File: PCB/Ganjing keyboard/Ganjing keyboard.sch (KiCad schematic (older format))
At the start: 166 parts, among them J1 Conn_01x04, J2 AVR-ISP-6, SW1 Rotary_Encoder_Switch, U1 ATmega32A-PU, Y1 Crystal

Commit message: Fixing PCB error
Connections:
- net Boot: no longer R1.2
- net Reset: now also R1.2
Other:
- moved on the sheet: R1, S1, S2
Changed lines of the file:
@@
 EESchema Schematic File Version 4
-LIBS:Ganjing keyboard-cache
 EELAYER 30 0
 EELAYER END
@@
 L power:GND #PWR019
 U 1 1 5F4DA3B8
-P 4750 7300
-F 0 "#PWR019" H 4750 7050 50  0001 C CNN
-F 1 "GND" H 4755 7127 50  0000 C CNN
-F 2 "" H 4750 7300 50  0001 C CNN
-F 3 "" H 4750 7300 50  0001 C CNN
-	1    4750 7300
+P 4800 7250
+F 0 "#PWR019" H 4800 7000 50  0001 C CNN
+F 1 "GND" H 4805 7077 50  0000 C CNN
+F 2 "" H 4800 7250 50  0001 C CNN
+F 3 "" H 4800 7250 50  0001 C CNN
+	1    4800 7250
 	1    0    0    -1
 $EndComp
-Text GLabel 5450 7200 2    50   Input ~ 0
+Text GLabel 5500 7150 2    50   Input ~ 0
 Reset
 $Comp
 L Ganjing-keyboard-rescue:1825910-7-dk_Tactile-Switches S2
 U 1 1 5F4DDD6B
-P 5150 7300
-F 0 "S2" H 5150 7647 60  0000 C CNN
-F 1 "Reset" H 5150 7541 60  0000 C CNN
-F 2 "digikey-footprints:Switch_Tactile_THT_6x6mm" H 5350 7500 60  0001 L CNN
-F 3 "https://www.te.com/commerce/DocumentDelivery/DDEController?Action=srchrtrv&DocNm=1825910&DocType=Customer+Drawing&DocLang=English" H 5350 7600 60  0001 L CNN
-F 4 "450-1804-ND" H 5350 7700 60  0001 L CNN "Digi-Key_PN"
-F 5 "1825910-7" H 5350 7800 60  0001 L CNN "MPN"
-F 6 "Switches" H 5350 7900 60  0001 L CNN "Category"
-F 7 "Tactile Switches" H 5350 8000 60  0001 L CNN "Family"
-F 8 "https://www.te.com/commerce/DocumentDelivery/DDEController?Action=srchrtrv&DocNm=1825910&DocType=Customer+Drawing&DocLang=English" H 5350 8100 60  0001 L CNN "DK_Datasheet_Link"
-F 9 "/product-detail/en/te-connectivity-alcoswitch-switches/1825910-7/450-1804-ND/1731414" H 5350 8200 60  0001 L CNN "DK_Detail_Page"
-F 10 "SWITCH TACTILE SPST-NO 0.05A 24V" H 5350 8300 60  0001 L CNN "Description"
-F 11 "TE Connectivity ALCOSWITCH Switches" H 5350 8400 60  0001 L CNN "Manufacturer"
-F 12 "Active" H 5350 8500 60  0001 L CNN "Status"
-	1    5150 7300
+P 5200 7250
+F 0 "S2" H 5200 7597 60  0000 C CNN
+F 1 "Reset" H 5200 7491 60  0000 C CNN
+F 2 "digikey-footprints:Switch_Tactile_THT_6x6mm" H 5400 7450 60  0001 L CNN
+F 3 "https://www.te.com/commerce/DocumentDelivery/DDEController?Action=srchrtrv&DocNm=1825910&DocType=Customer+Drawing&DocLang=English" H 5400 7550 60  0001 L CNN
+F 4 "450-1804-ND" H 5400 7650 60  0001 L CNN "Digi-Key_PN"
+F 5 "1825910-7" H 5400 7750 60  0001 L CNN "MPN"
+F 6 "Switches" H 5400 7850 60  0001 L CNN "Category"
+F 7 "Tactile Switches" H 5400 7950 60  0001 L CNN "Family"
+F 8 "https://www.te.com/commerce/DocumentDelivery/DDEController?Action=srchrtrv&DocNm=1825910&DocType=Customer+Drawing&DocLang=English" H 5400 8050 60  0001 L CNN "DK_Datasheet_Link"
+F 9 "/product-detail/en/te-connectivity-alcoswitch-switches/1825910-7/450-1804-ND/1731414" H 5400 8150 60  0001 L CNN "DK_Detail_Page"
+F 10 "SWITCH TACTILE SPST-NO 0.05A 24V" H 5400 8250 60  0001 L CNN "Description"
+F 11 "TE Connectivity ALCOSWITCH Switches" H 5400 8350 60  0001 L CNN "Manufacturer"
+F 12 "Active" H 5400 8450 60  0001 L CNN "Status"
+	1    5200 7250
 	1    0    0    -1
 $EndComp
 Wire Wire Line
-	4750 7200 4750 7300
-Wire Wire Line
-	5350 7200 5450 7200
-Wire Wire Line
-	4750 7200 4950 7200
-NoConn ~ 5350 7400
-NoConn ~ 4950 7400
+	4800 7150 4800 7250
+Wire Wire Line
+	5400 7150 5450 7150
+Wire Wire Line
+	4800 7150 5000 7150
+NoConn ~ 5400 7350
+NoConn ~ 5000 7350
 $Comp
 L Ganjing-keyboard-rescue:1825910-7-dk_Tactile-Switches S1
 U 1 1 5F4E706C
-P 5150 6600
-F 0 "S1" H 5150 6947 60  0000 C CNN
-F 1 "Boot" H 5150 6841 60  0000 C CNN
-F 2 "digikey-footprints:Switch_Tactile_THT_6x6mm" H 5350 6800 60  0001 L CNN
-F 3 "https://www.te.com/commerce/DocumentDelivery/DDEController?Action=srchrtrv&DocNm=1825910&DocType=Customer+Drawing&DocLang=English" H 5350 6900 60  0001 L CNN
-F 4 "450-1804-ND" H 5350 7000 60  0001 L CNN "Digi-Key_PN"
-F 5 "1825910-7" H 5350 7100 60  0001 L CNN "MPN"
-F 6 "Switches" H 5350 7200 60  0001 L CNN "Category"
-F 7 "Tactile Switches" H 5350 7300 60  0001 L CNN "Family"
-F 8 "https://www.te.com/commerce/DocumentDelivery/DDEController?Action=srchrtrv&DocNm=1825910&DocType=Customer+Drawing&DocLang=English" H 5350 7400 60  0001 L CNN "DK_Datasheet_Link"
-F 9 "/product-detail/en/te-connectivity-alcoswitch-switches/1825910-7/450-1804-ND/1731414" H 5350 7500 60  0001 L CNN "DK_Detail_Page"
-F 10 "SWITCH TACTILE SPST-NO 0.05A 24V" H 5350 7600 60  0001 L CNN "Description"
-F 11 "TE Connectivity ALCOSWITCH Switches" H 5350 7700 60  0001 L CNN "Manufacturer"
-F 12 "Active" H 5350 7800 60  0001 L CNN "Status"
-	1    5150 6600
+P 5200 6300
+F 0 "S1" H 5200 6647 60  0000 C CNN
+F 1 "Boot" H 5200 6541 60  0000 C CNN
+F 2 "digikey-footprints:Switch_Tactile_THT_6x6mm" H 5400 6500 60  0001 L CNN
+F 3 "https://www.te.com/commerce/DocumentDelivery/DDEController?Action=srchrtrv&DocNm=1825910&DocType=Customer+Drawing&DocLang=English" H 5400 6600 60  0001 L CNN
+F 4 "450-1804-ND" H 5400 6700 60  0001 L CNN "Digi-Key_PN"
+F 5 "1825910-7" H 5400 6800 60  0001 L CNN "MPN"
+F 6 "Switches" H 5400 6900 60  0001 L CNN "Category"
+F 7 "Tactile Switches" H 5400 7000 60  0001 L CNN "Family"
+F 8 "https://www.te.com/commerce/DocumentDelivery/DDEController?Action=srchrtrv&DocNm=1825910&DocType=Customer+Drawing&DocLang=English" H 5400 7100 60  0001 L CNN "DK_Datasheet_Link"
+F 9 "/product-detail/en/te-connectivity-alcoswitch-switches/1825910-7/450-1804-ND/1731414" H 5400 7200 60  0001 L CNN "DK_Detail_Page"
+F 10 "SWITCH TACTILE SPST-NO 0.05A 24V" H 5400 7300 60  0001 L CNN "Description"
+F 11 "TE Connectivity ALCOSWITCH Switches" H 5400 7400 60  0001 L CNN "Manufacturer"
+F 12 "Active" H 5400 7500 60  0001 L CNN "Status"
+	1    5200 6300
 	1    0    0    -1
 $EndComp
-Text GLabel 5450 6500 2    50   Input ~ 0
+Text GLabel 5500 6200 2    50   Input ~ 0
 Boot
 Wire Wire Line
-	5350 6500 5400 6500
+	5000 6200 4800 6200
 Wire Wire Line
-	4950 6500 4750 6500
+	4800 6200 4800 6300
 Wire Wire Line
-	4750 6500 4750 6600
-$Comp
-L power:+5V #PWR014
-U 1 1 5F4E9317
-P 5400 6100
-F 0 "#PWR014" H 5400 5950 50  0001 C CNN
-F 1 "+5V" H 5415 6273 50  0000 C CNN
-F 2 "" H 5400 6100 50  0001 C CNN
-F 3 "" H 5400 6100 50  0001 C CNN
-	1    5400 6100
-	1    0    0    -1
-$EndComp
-$Comp
-L Device:R_Small R1
-U 1 1 5F4E9D5C
-P 5400 6300
-F 0 "R1" H 5459 6346 50  0000 L CNN
-F 1 "10k" H 5459 6255 50  0000 L CNN
-F 2 "Resistor_THT:R_Axial_DIN0204_L3.6mm_D1.6mm_P5.08mm_Horizontal" H 5400 6300 50  0001 C CNN
-F 3 "https://www.mouser.com/datasheet/2/447/Yageo_LR_MFR_1-1714151.pdf" H 5400 6300 50  0001 C CNN
-F 4 "603-MFR-12FTF52-10K" H 5400 6300 50  0001 C CNN "Field4"
-F 5 "https://www.mouser.com/ProductDetail/Yageo/MFR-12FTF52-10K?qs=oAGoVhmvjhzLlUYKKBtdYQ%3D%3D" H 5400 6300 50  0001 C CNN "Mouser link"
-	1    5400 6300
-	1    0    0    -1
-$EndComp
-Wire Wire Line
-	5400 6100 5400 6200
-Wire Wire Line
-	5400 6400 5400 6500
-Connection ~ 5400 6500
-Wire Wire Line
-	5400 6500 5450 6500
+	5450 6750 5450 6850
 Text GLabel 4200 6500 2    50   Input ~ 0
 D+
@@
 	1    0    0    -1
 $EndComp
-NoConn ~ 5350 6700
-NoConn ~ 4950 6700
+NoConn ~ 5400 6400
+NoConn ~ 5000 6400
 Text GLabel 2650 2150 2    50   Input ~ 0
 col7
@@
 L power:GND #PWR0101
 U 1 1 5F5C998A
-P 4750 6600
-F 0 "#PWR0101" H 4750 6350 50  0001 C CNN
-F 1 "GND" H 4755 6427 50  0000 C CNN
-F 2 "" H 4750 6600 50  0001 C CNN
-F 3 "" H 4750 6600 50  0001 C CNN
-	1    4750 6600
+P 4800 6300
+F 0 "#PWR0101" H 4800 6050 50  0001 C CNN
+F 1 "GND" H 4805 6127 50  0000 C CNN
+F 2 "" H 4800 6300 50  0001 C CNN
+F 3 "" H 4800 6300 50  0001 C CNN
+	1    4800 6300
 	1    0    0    -1
 $EndComp
+$Comp
+L power:+5V #PWR014
+U 1 1 5F4E9317
+P 5450 6750
+F 0 "#PWR014" H 5450 6600 50  0001 C CNN
+F 1 "+5V" H 5465 6923 50  0000 C CNN
+F 2 "" H 5450 6750 50  0001 C CNN
+F 3 "" H 5450 6750 50  0001 C CNN
+	1    5450 6750
+	1    0    0    -1
+$EndComp
+$Comp
+L Device:R_Small R1
+U 1 1 5F4E9D5C
+P 5450 6950
+F 0 "R1" H 5509 6996 50  0000 L CNN
+F 1 "10k" H 5509 6905 50  0000 L CNN
+F 2 "Resistor_THT:R_Axial_DIN0204_L3.6mm_D1.6mm_P5.08mm_Horizontal" H 5450 6950 50  0001 C CNN
+F 3 "https://www.mouser.com/datasheet/2/447/Yageo_LR_MFR_1-1714151.pdf" H 5450 6950 50  0001 C CNN
+F 4 "603-MFR-12FTF52-10K" H 5450 6950 50  0001 C CNN "Field4"
+F 5 "https://www.mouser.com/ProductDetail/Yageo/MFR-12FTF52-10K?qs=oAGoVhmvjhzLlUYKKBtdYQ%3D%3D" H 5450 6950 50  0001 C CNN "Mouser link"
+	1    5450 6950
+	1    0    0    -1
+$EndComp
+Wire Wire Line
+	5400 6200 5500 6200
+Wire Wire Line
+	5450 7050 5450 7150
+Connection ~ 5450 7150
+Wire Wire Line
+	5450 7150 5500 7150
 $EndSCHEMATC

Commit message: Updating gerbers
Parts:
- D68: value Caps lock -> Caps
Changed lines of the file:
@@
 P 10250 5850
 F 0 "D68" H 10243 6066 50  0000 C CNN
-F 1 "Caps lock" H 10243 5975 50  0000 C CNN
+F 1 "Caps" H 10243 5975 50  0000 C CNN
 F 2 "Keyboard:LED_D3.0mm" H 10250 5850 50  0001 C CNN
 F 3 "https://media.digikey.com/pdf/Data%20Sheets/Lite-On%20PDFs/LTL-4232N.pdf" H 10250 5850 50  0001 C CNN

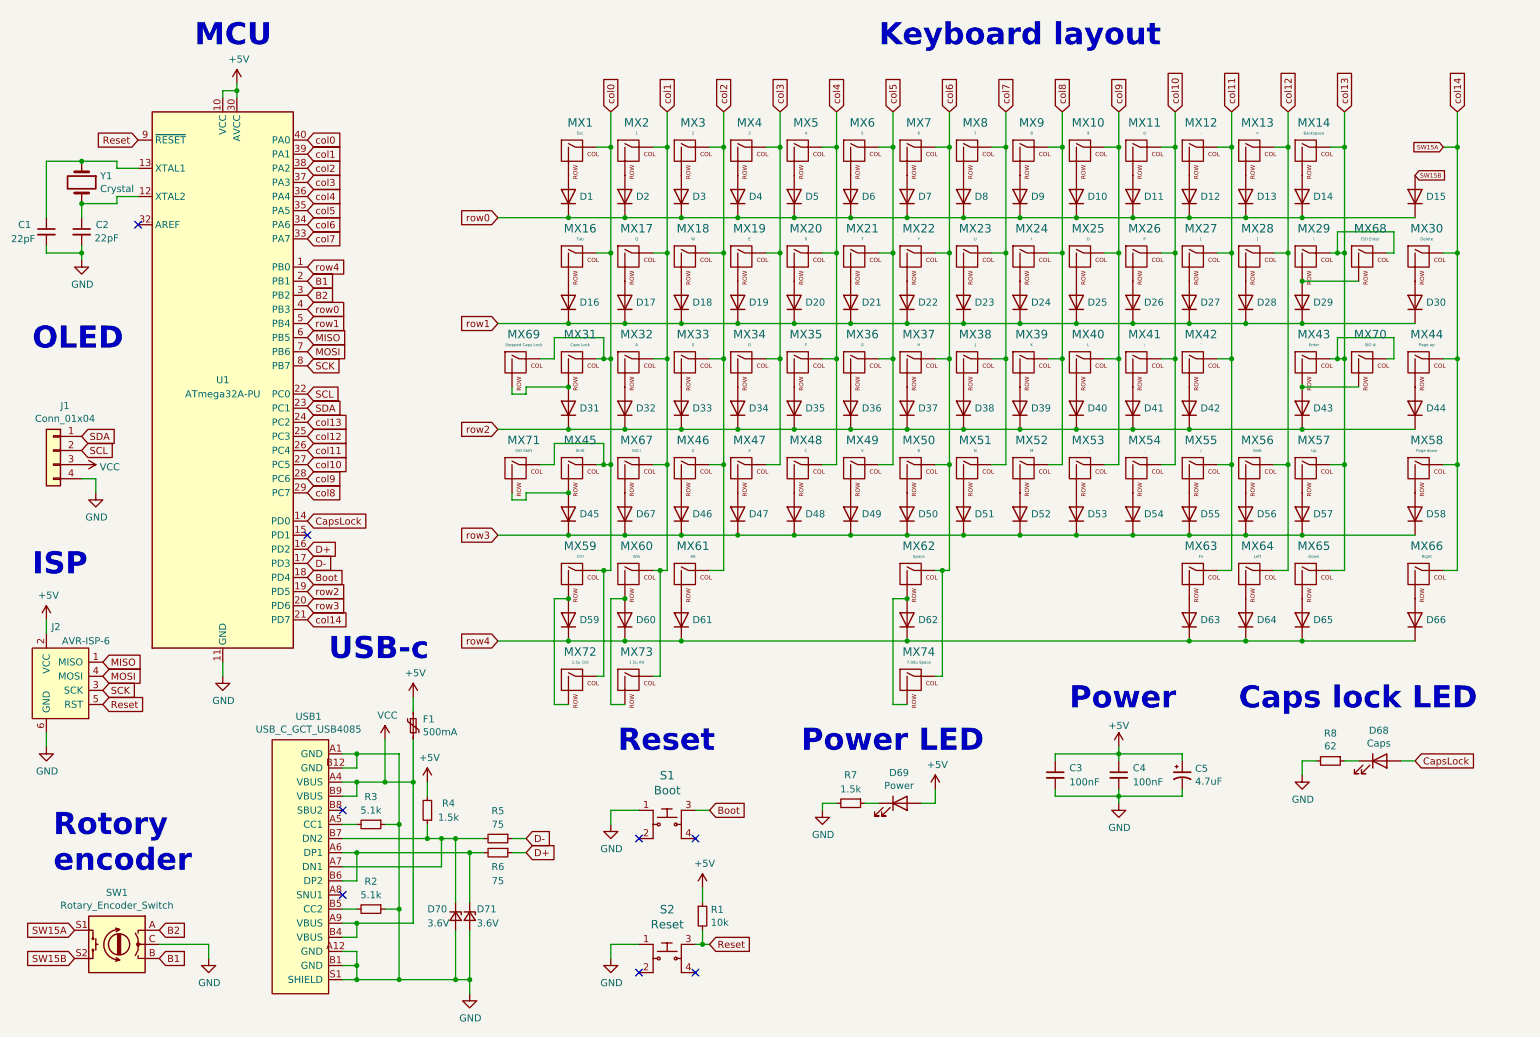
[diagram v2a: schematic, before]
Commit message: Removing caps lock LED
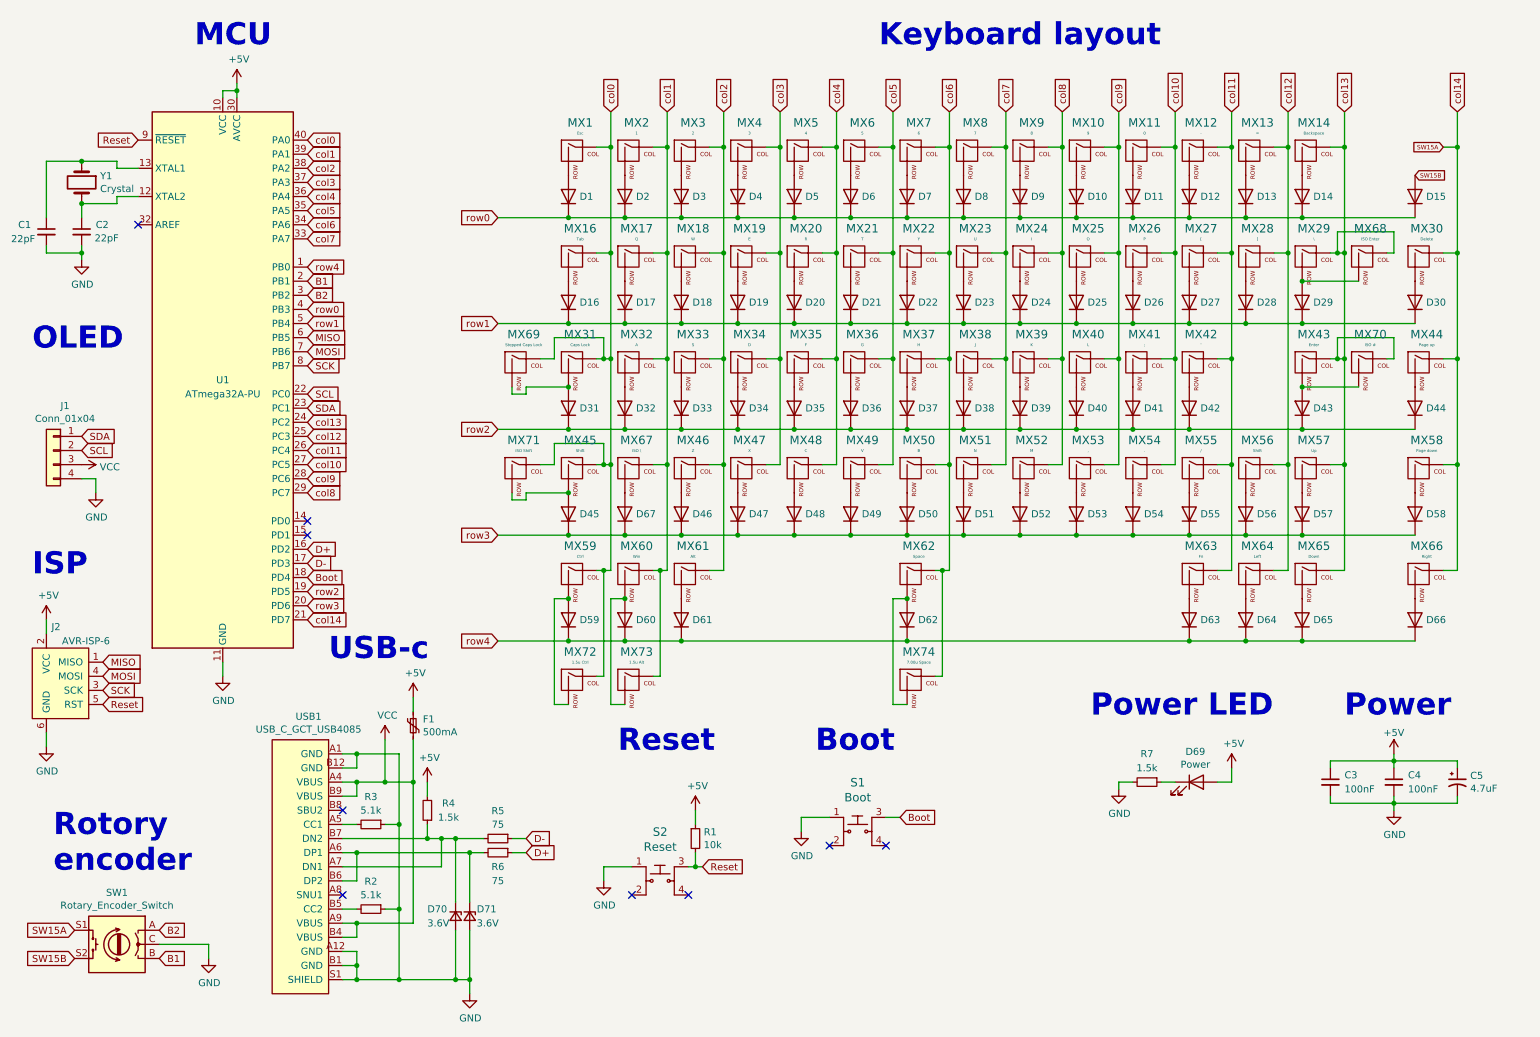
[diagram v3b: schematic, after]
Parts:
- removed D68: Caps, Keyboard:LED_D3.0mm, symbol Device:LED
- removed R8: 62, Resistor_THT:R_Axial_DIN0204_L3.6mm_D1.6mm_P5.08mm_Horizontal, symbol Device:R_Small
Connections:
- net CapsLock: no longer names the net of U1.14 (PD0)
- no-connect marks 8 -> 9
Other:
- note added: "Boot"
- note removed: "Caps lock LED"
- moved on the sheet: C3, C4, C5, D69, R1, R7, S1, S2

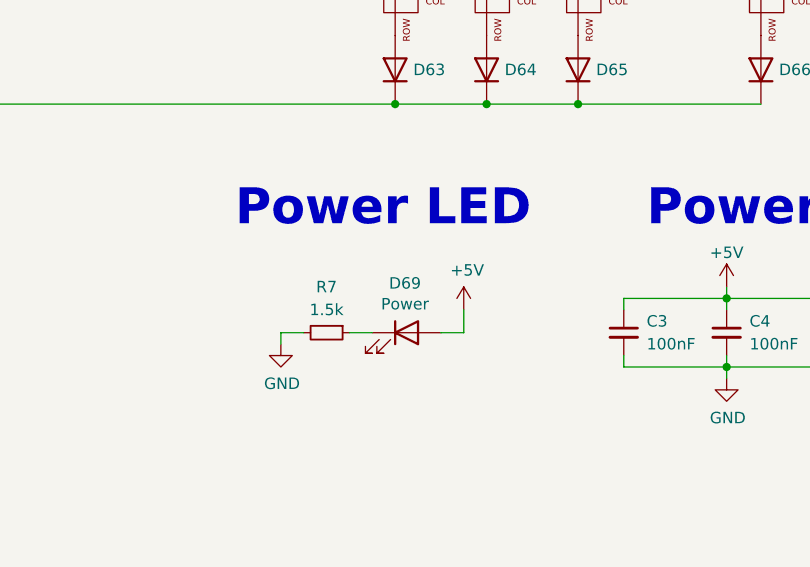
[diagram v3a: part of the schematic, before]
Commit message: Updating images and generating new gerbers
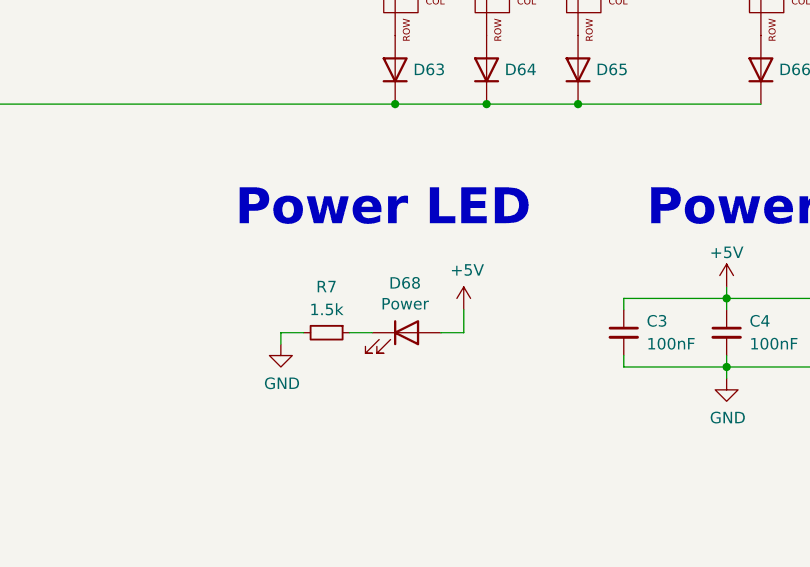
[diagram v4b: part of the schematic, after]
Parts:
- renumbered D69 to D68
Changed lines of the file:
@@
 	9200 5900 9200 6000
 $Comp
-L Device:LED D69
+L Device:LED D68
 U 1 1 5F4D0275
 P 8950 6000
-F 0 "D69" H 8943 6216 50  0000 C CNN
+F 0 "D68" H 8943 6216 50  0000 C CNN
 F 1 "Power" H 8943 6125 50  0000 C CNN
 F 2 "Keyboard:LED_D3.0mm" H 8950 6000 50  0001 C CNN

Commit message: Adding 3d models
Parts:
- Y1: footprint GanJing-crystal:CTS-ATS16B-0 -> Keyboard:Crystal_HC49-4H_Vertical
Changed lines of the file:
@@
 F 0 "Y1" V 1004 1881 50  0000 L CNN
 F 1 "Crystal" V 1095 1881 50  0000 L CNN
-F 2 "GanJing-crystal:CTS-ATS16B-0" H 1050 1750 50  0001 C CNN
+F 2 "Keyboard:Crystal_HC49-4H_Vertical" H 1050 1750 50  0001 C CNN
 F 3 "https://www.mouser.com/datasheet/2/3/ABL-1774766.pdf" H 1050 1750 50  0001 C CNN
 F 4 "815-ABL16000MHZB4YT" V 1050 1750 50  0001 C CNN "Mouser #"
